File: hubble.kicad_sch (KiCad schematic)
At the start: 97 parts, among them J1 USB3_A_LCSC, J2 USB3_A_LCSC, J3 USB_C_Receptacle_Molex, J5 USB3_A_LCSC, J6 USB3_A_LCSC, J7 USB3_A_LCSC, J8 USB3_A_LCSC, J9 Conn_02x02_Odd_Even, SW1 K3-2235D-F1, U1 MAX6816EUS+T, U10 TPD1E05U06DPY, U11 TPD1E05U06DPY, U12 TPD1E05U06DPY, U13 TPD1E05U06DPY, U2 TPD1E05U06DPY, U3 TS3USB221RSER, U4 TPS7A5201QRGRRQ1, U5 USB5744, U6 TPS7A5201QRGRRQ1, U7 FUSB340, U8 TPD1E05U06DPY, U9 TPD1E05U06DPY, Y1 X322525MOB4SI

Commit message: Add ki-lime-pi-to-go submodule, upgrade to KiCad 9, put a Pico W and through hole header on the schematic
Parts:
- added A1: RaspberryPi_Pico_W, Module_RaspberryPi_Pico:RaspberryPi_Pico_Common_THT, symbol MCU_Module_RaspberryPi_Pico:RaspberryPi_Pico_W_SecondaryPins
- added J10: Pico_Socket_B, Module_RaspberryPi_Pico:RaspberryPi_Pico_PinSocket_1x20_P2.54mm_Vertical, symbol MCU_Module_RaspberryPi_Pico:RaspberryPi_Pico_MultiPart-Socket_B
- added J4: Pico_Socket_A, Module_RaspberryPi_Pico:RaspberryPi_Pico_PinSocket_1x20_P2.54mm_Vertical, symbol MCU_Module_RaspberryPi_Pico:RaspberryPi_Pico_MultiPart-Socket_A
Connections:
- new net: A1.1 (GPIO0), J4.1 (GPIO0)
- new net: A1.10 (GPIO7), J4.10 (GPIO7)
- new net: A1.11 (GPIO8), J4.11 (GPIO8)
- new net: A1.12 (GPIO9), J4.12 (GPIO9)
- new net: A1.13 (GND), A1.18 (GND), A1.23 (GND), A1.28 (GND), A1.3 (GND), A1.38 (GND), A1.8 (GND), A1.D2 (GND), J10.18 (GND), J10.3 (GND), J10.8 (GND), J4.13 (GND), J4.18 (GND), J4.3 (GND), J4.8 (GND)
- new net: A1.14 (GPIO10), J4.14 (GPIO10)
- new net: A1.15 (GPIO11), J4.15 (GPIO11)
- new net: A1.16 (GPIO12), J4.16 (GPIO12)
- new net: A1.17 (GPIO13), J4.17 (GPIO13)
- new net: A1.19 (GPIO14), J4.19 (GPIO14)
- new net: A1.2 (GPIO1), J4.2 (GPIO1)
- new net: A1.20 (GPIO15), J4.20 (GPIO15)
- new net: A1.4 (GPIO2), J4.4 (GPIO2)
- new net: A1.5 (GPIO3), J4.5 (GPIO3)
- new net: A1.6 (GPIO4), J4.6 (GPIO4)
- new net: A1.7 (GPIO5), J4.7 (GPIO5)
- new net: A1.9 (GPIO6), J4.9 (GPIO6)
- new net: A1.21 (GPIO16), J10.1 (GPIO16)
- new net: A1.30 (RUN), J10.10 (RUN)
- new net: A1.31 (GPIO26_ADC0), J10.11 (GPIO26_ADC0)
- new net: A1.32 (GPIO27_ADC1), J10.12 (GPIO27_ADC1)
- new net: A1.33 (AGND), J10.13 (AGND)
- new net: A1.34 (GPIO28_ADC2), J10.14 (GPIO28_ADC2)
- new net: A1.35 (ADC_VREF), J10.15 (ADC_VREF)
- new net: A1.36 (3V3), J10.16 (3V3)
- new net: A1.37 (3V3_EN), J10.17 (3V3_EN)
- new net: A1.39 (VSYS), J10.19 (VSYS)
- new net: A1.22 (GPIO17), J10.2 (GPIO17)
- new net: A1.40 (VBUS), J10.20 (VBUS)
- new net: A1.24 (GPIO18), J10.4 (GPIO18)
- new net: A1.25 (GPIO19), J10.5 (GPIO19)
- new net: A1.26 (GPIO20), J10.6 (GPIO20)
- new net: A1.27 (GPIO21), J10.7 (GPIO21)
- new net: A1.29 (GPIO22), J10.9 (GPIO22)
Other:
- moved on the sheet: C1, C10, C11, C12, C13, C14, C15, C16, C17, C18, C19, C2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

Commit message: Add 2:1 displayport mux using TS3DV642
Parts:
- removed J9: Conn_02x02_Odd_Even, Connector_PinHeader_2.54mm:PinHeader_2x02_P2.54mm_Vertical, symbol Connector_Generic:Conn_02x02_Odd_Even
- added C49, C5, C50, C51, C52, C53, C54, C55: 0.1uF, Capacitor_SMD:C_0603_1608Metric, symbol Device:C_Small
- added J11, J12, J9: DisplayPort, hubble:DISPLAYPORT_XDPF-0205-20S, symbol hubble:DisplayPort
- added R11, R25: 10k, Resistor_SMD:R_0603_1608Metric, symbol Device:R
- added R12, R28: 1M, Resistor_SMD:R_0603_1608Metric, symbol Device:R
- added R26, R27: 100k, Resistor_SMD:R_0603_1608Metric, symbol Device:R
- added R29, R6, R9: 330, Resistor_SMD:R_0603_1608Metric, symbol Device:R
- added TP10, TP11, TP12, TP13, TP14, TP8, TP9: TestPoint, TestPoint:TestPoint_Pad_1.0x1.0mm, symbol Connector:TestPoint
- added U14: TS3DV642A0RUAR, hubble:TS3DV642, symbol hubble:TS3DV642A0RUAR
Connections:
- net GND: now also C49.1, C5.1, C50.1, C55.1, J11.11 (GND), J11.16 (GND), J11.2 (GND), J11.5 (GND), J11.8 (GND), J12.19 (DP_PWR_RET), J12.SH, J9.11 (GND), J9.16 (GND), J9.2 (GND), J9.5 (GND), J9.8 (GND), R11.2, R12.2, R26.2, R28.2, R29.2, R6.2, R9.2, U14.43 (GND)
- net I2C_SCL: now also R14.2; no longer R17.2
- net I2C_SDA: now also R17.2; no longer R14.2
- net MUX_SEL: now also R11.1, U14.17 (SEL2)
- net Shield: now also C49.2, C5.2, C55.2, J11.SH, J12.11 (GND), J12.16 (GND), J12.2 (GND), J12.5 (GND), J12.8 (GND), J9.SH, R29.1, R6.1, R9.1
- net VCC_3.3V: now also C50.2, J12.20 (DP_PWR), R25.1, R27.1, U14.1 (VCC), U14.2 (EN)
- new net: J11.13 (CFG1), TP11.1
- new net: J11.14 (CFG2), TP12.1
- new net: C54.1, J11.15 (AUX_P)
- new net: C53.1, J11.17 (AUX_N)
- new net: J12.13 (CFG1), R28.1
- new net: J9.14 (CFG2), TP14.1
- new net: C51.1, J9.15 (AUX_P)
- new net: J12.14 (CFG2), R12.1
- new net: TP9.1, U14.20 (CEC_B)
- new net: C52.1, J9.17 (AUX_N)
- new net: TP10.1, U14.15 (CEC)
- new net: R25.2, U14.16 (SEL1)
- new net: TP8.1, U14.18 (CEC_A)
- new net: J9.13 (CFG1), TP13.1
- new net DP_HOST0_AUX_N: C52.2, U14.41 (SDA_A)
- new net DP_HOST0_AUX_P: C51.2, U14.42 (SCL_A)
- new net DP_HOST0_D0_N: J9.3 (D0_N), U14.37 (D0-A)
- new net DP_HOST0_D0_P: J9.1 (D0_P), U14.38 (D0+A)
- new net DP_HOST0_D1_N: J9.6 (D1_N), U14.35 (D1-A)
- new net DP_HOST0_D1_P: J9.4 (D1_P), U14.36 (D1+A)
- new net DP_HOST0_D2_N: J9.9 (D2_N), U14.33 (D2-A)
- new net DP_HOST0_D2_P: J9.7 (D2_P), U14.34 (D2+A)
- new net DP_HOST0_D3_N: J9.12 (D3_N), U14.31 (D3-A)
- new net DP_HOST0_D3_P: J9.10 (D3_P), U14.32 (D3+A)
- new net DP_HOST0_HPD: J9.18 (HPD), U14.19 (HPD_A)
- new net DP_HOST1_AUX_N: C53.2, U14.39 (SDA_B)
- new net DP_HOST1_AUX_P: C54.2, U14.40 (SCL_B)
- new net DP_HOST1_D0_N: J11.3 (D0_N), U14.28 (D0-B)
- new net DP_HOST1_D0_P: J11.1 (D0_P), U14.29 (D0+B)
- new net DP_HOST1_D1_N: J11.6 (D1_N), U14.26 (D1-B)
- new net DP_HOST1_D1_P: J11.4 (D1_P), U14.27 (D1+B)
- new net DP_HOST1_D2_N: J11.9 (D2_N), U14.24 (D2-B)
- new net DP_HOST1_D2_P: J11.7 (D2_P), U14.25 (D2+B)
- new net DP_HOST1_D3_N: J11.12 (D3_N), U14.22 (D3-B)
- new net DP_HOST1_D3_P: J11.10 (D3_P), U14.23 (D3+B)
- new net DP_HOST1_HPD: J11.18 (HPD), U14.21 (HPD_B)
- new net DP_SINK_AUX_N: J12.17 (AUX_N), R27.2, U14.4 (SDA)
- new net DP_SINK_AUX_P: J12.15 (AUX_P), R26.1, U14.3 (SCL)
- new net DP_SINK_D0_N: J12.12 (D3_N), U14.6 (D0-)
- new net DP_SINK_D0_P: J12.10 (D3_P), U14.5 (D0+)
- new net DP_SINK_D1_N: J12.9 (D2_N), U14.8 (D1-)
- new net DP_SINK_D1_P: J12.7 (D2_P), U14.7 (D1+)
- new net DP_SINK_D2_N: J12.6 (D1_N), U14.11 (D2-)
- new net DP_SINK_D2_P: J12.4 (D1_P), U14.10 (D2+)
- new net DP_SINK_D3_N: J12.3 (D0_N), U14.13 (D3-)
- new net DP_SINK_D3_P: J12.1 (D0_P), U14.12 (D3+)
- new net DP_SINK_HPD: J12.18 (HPD), U14.14 (HPD)
- no-connect marks 21 -> 26
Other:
- note added: "HOST0 by default"
- note added: "Since we have 2 cables, un-flip the data lanes"
- note added: "TODO: check these PUs/PDs"
- note removed: "Shortened TotalPhase Aardvark debug connector"
- moved on the sheet: A1, C1, C10, C11, C12, C13, C14, C15, C16, C17, C18, C19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

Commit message: Use 2x FUSB340 mux for DisplayPort, break up schematic into hierarchical pages
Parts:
- removed A1: RaspberryPi_Pico_W, Module_RaspberryPi_Pico:RaspberryPi_Pico_Common_THT, symbol MCU_Module_RaspberryPi_Pico:RaspberryPi_Pico_W_SecondaryPins
- removed C1, C10, C11, C12, C14, C15, C16, C17, C18, C19, C20, C21, C22, C23, C24, C25, C27, C28, C29, C30, C31, C32, C34, C35, C37, C38, C39, C40, C41, C42, C43, C44, C49, C5, C50, C51, C52, C53, C54, C55, C6, C7, C8, C9: 0.1uF, Capacitor_SMD:C_0603_1608Metric, symbol Device:C_Small
- removed C13, C33: 10uF, Capacitor_SMD:C_0603_1608Metric, symbol Device:C_Small
- removed C2, C45, C46, C47, C48: 2.2uF, Capacitor_SMD:C_0603_1608Metric, symbol Device:C_Small
- removed C26, C36: 22uF, Capacitor_SMD:C_0603_1608Metric, symbol Device:C_Small
- removed C3, C4: 20pF, Capacitor_SMD:C_0603_1608Metric, symbol Device:C_Small
- removed J1, J2, J5, J6, J7, J8: USB3_A_LCSC, hubble:USB-TH_XUNPU_USB-301WD-ARY, symbol hubble:USB3_A_LCSC
- removed J10: Pico_Socket_B, Module_RaspberryPi_Pico:RaspberryPi_Pico_PinSocket_1x20_P2.54mm_Vertical, symbol MCU_Module_RaspberryPi_Pico:RaspberryPi_Pico_MultiPart-Socket_B
- removed J11, J12, J9: DisplayPort, hubble:DISPLAYPORT_XDPF-0205-20S, symbol hubble:DisplayPort
- removed J3: USB_C_Receptacle_Molex, hubble:USB_C_CONN_105450-0101_MOLEX, symbol hubble:USB_C_Receptacle_Molex
- removed J4: Pico_Socket_A, Module_RaspberryPi_Pico:RaspberryPi_Pico_PinSocket_1x20_P2.54mm_Vertical, symbol MCU_Module_RaspberryPi_Pico:RaspberryPi_Pico_MultiPart-Socket_A
- removed R1, R29, R6, R9: 330, Resistor_SMD:R_0603_1608Metric, symbol Device:R
- removed R10, R11, R13, R14, R17, R25: 10k, Resistor_SMD:R_0603_1608Metric, symbol Device:R
- removed R12, R28: 1M, Resistor_SMD:R_0603_1608Metric, symbol Device:R
- removed R15: 11.8k, Resistor_SMD:R_0603_1608Metric, symbol Device:R
- removed R16: 3.74k, Resistor_SMD:R_0603_1608Metric, symbol Device:R
- removed R18, R24, R7: 50k, Resistor_SMD:R_0603_1608Metric, symbol Device:R
- removed R19: 12k, Resistor_SMD:R_0603_1608Metric, symbol Device:R
- removed R2, R3: 5.1k, Resistor_SMD:R_0603_1608Metric, symbol Device:R
- removed R20, R21: 200k, Resistor_SMD:R_0603_1608Metric, symbol Device:R
- removed R22: 12.4k, Resistor_SMD:R_0603_1608Metric, symbol Device:R
- removed R23: 24.9k, Resistor_SMD:R_0603_1608Metric, symbol Device:R
- removed R26, R27, R8: 100k, Resistor_SMD:R_0603_1608Metric, symbol Device:R
- removed R4, R5: 0, Resistor_SMD:R_0603_1608Metric, symbol Device:R
- removed SW1: K3-2235D-F1, hubble:SW-TH_K3-2235D-F1, symbol Switch:SW_Push_DPDT
- removed TP1, TP10, TP11, TP12, TP13, TP14, TP2, TP3, TP4, TP5, TP6, TP7, TP8, TP9: TestPoint, TestPoint:TestPoint_Pad_1.0x1.0mm, symbol Connector:TestPoint
- removed U1: MAX6816EUS+T, Package_TO_SOT_SMD:SOT-143, symbol Interface:MAX6816
- removed U10, U11, U12, U13, U2, U8, U9: TPD1E05U06DPY, Package_SON:Texas_DPY0002A_0.6x1mm_P0.65mm, symbol Power_Protection:TPD1E05U06DPY
- removed U14: TS3DV642A0RUAR, hubble:TS3DV642, symbol hubble:TS3DV642A0RUAR
- removed U3: TS3USB221RSER, hubble:UQFN-10, symbol hubble:SN080104RSER
- removed U4, U6: TPS7A5201QRGRRQ1, hubble:RGR20_2P05X2P05_TEX, symbol hubble:TPS7A5201QRGRRQ1
- removed U5: USB5744, hubble:VQFN56_2G_MCH, symbol hubble:USB5744-I_2G
- removed U7: FUSB340, hubble:TMLP-18_L2.8-W2.0-P0.40-BL-EP, symbol hubble:FUSB340TMX
- removed Y1: X322525MOB4SI, Crystal:Crystal_SMD_3225-4Pin_3.2x2.5mm, symbol Device:Crystal_GND24_Small
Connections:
- no-connect marks 26 -> 0
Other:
- added sheet DisplayPort (displayport.kicad_sch)
- added sheet Hub (hub.kicad_sch)
- added sheet MCU (mcu.kicad_sch)
- added sheet Power (power.kicad_sch)
- note removed: "1%"
- note removed: "1.2V LDO"
- note removed: "1D+/- by default"
- note removed: "25MHz"
- note removed: "3.3V LDO"
- note removed: "HOST 1"
- note removed: "HOST 2"
- note removed: "HOST0 by default"
- note removed: "IN"
- note removed: "If I get bored and want to make a USB-C debug board..."
- note removed: "Not using a PD controller for now Assuming Type-C power supplies simply have enough oomph"
- note removed: "OUT"
- note removed: "Since we have 2 cables, un-flip the data lanes"
- note removed: "TODO: check these PUs/PDs"
- note removed: "TX1/RX1 by default"
- note removed: "VBUS_DET into USB5744 should be 3.3V or 0V"

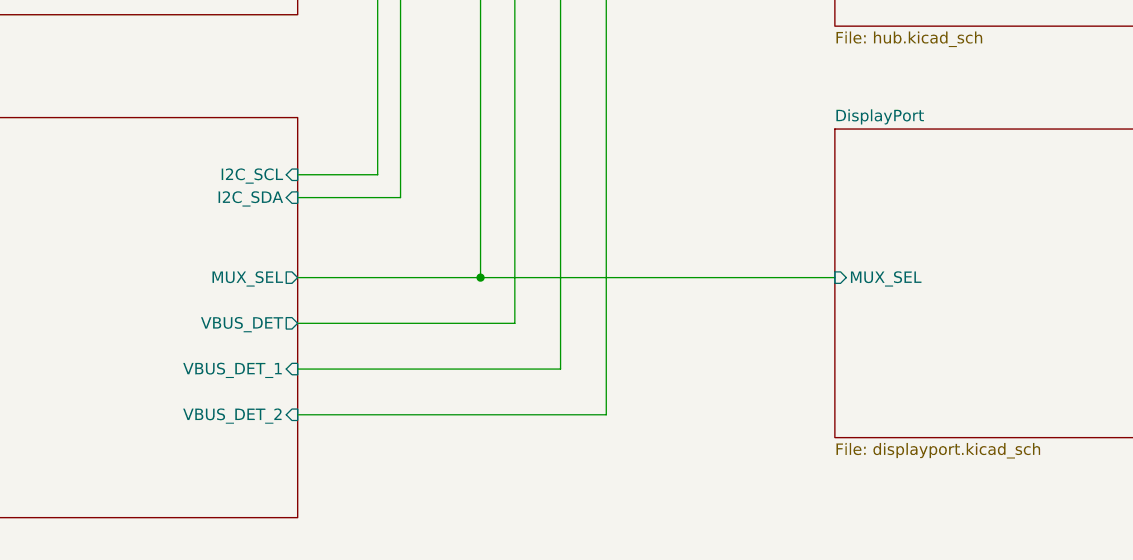
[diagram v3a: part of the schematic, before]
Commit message: Start wiring up Pi Pico
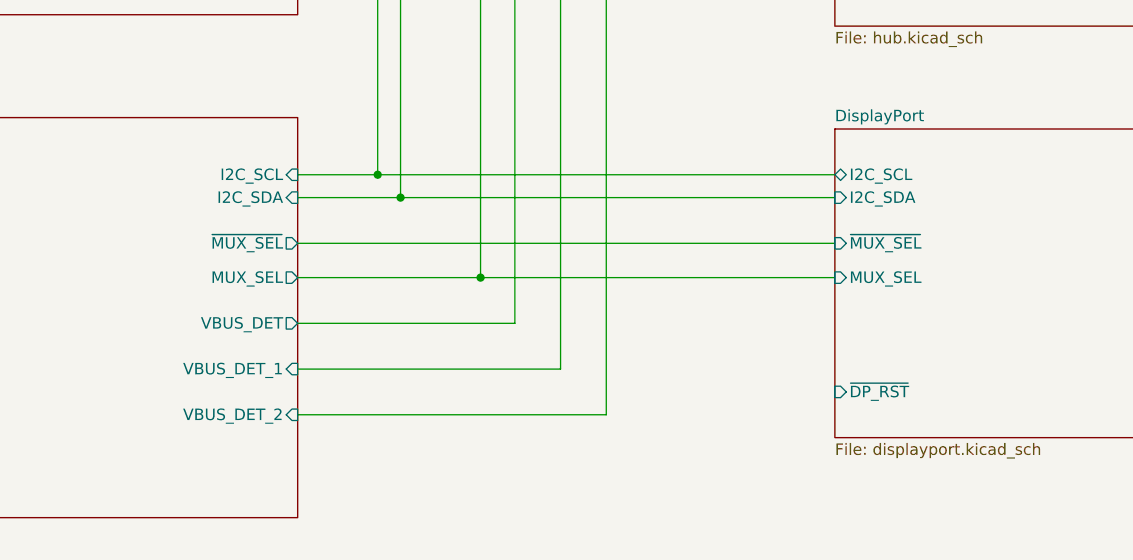
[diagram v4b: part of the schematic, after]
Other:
- sheet DisplayPort ports: added I2C_SCL, I2C_SDA, ~{DP_RST}, ~{MUX_SEL}; removed none
- sheet MCU ports: added ~{MUX_SEL}; removed none
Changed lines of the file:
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@@
+	)
+	(junction
+		(at 205.74 160.02)
+		(diameter 0)
+		(color 0 0 0 0)
 	)
 	(junction
@@
 	)
 	(junction
+		(at 203.2 157.48)
+		(diameter 0)
+		(color 0 0 0 0)
+	)
+	(junction
 		(at 214.63 168.91)
 		(diameter 0)
@@
 	(wire
 		(pts
+			(xy 194.31 165.1) (xy 254 165.1)
+		)
+		(stroke
+			(width 0)
+			(type default)
+		)
+	)
+	(wire
+		(pts
 			(xy 214.63 168.91) (xy 254 168.91)
 		)
@@
 	(wire
 		(pts
+			(xy 203.2 157.48) (xy 254 157.48)
+		)
+		(stroke
+			(width 0)
+			(type default)
+		)
+	)
+	(wire
+		(pts
 			(xy 194.31 179.07) (xy 223.52 179.07)
 		)
@@
 		(pts
 			(xy 254 119.38) (xy 218.44 119.38)
+		)
+		(stroke
+			(width 0)
+			(type default)
+		)
+	)
+	(wire
+		(pts
+			(xy 205.74 160.02) (xy 254 160.02)
 		)
 		(stroke
@@
 			)
 		)
+		(pin "I2C_SCL" bidirectional
+			(at 254 157.48 180)
+			(effects
+				(font
+					(size 1.27 1.27)
+				)
+				(justify left)
+			)
+		)
+		(pin "I2C_SDA" input
+			(at 254 160.02 180)
+			(effects
+				(font
+					(size 1.27 1.27)
+				)
+				(justify left)
+			)
+		)
+		(pin "~{DP_RST}" input
+			(at 254 181.61 180)
+			(effects
+				(font
+					(size 1.27 1.27)
+				)
+				(justify left)
+			)
+		)
+		(pin "~{MUX_SEL}" input
+			(at 254 165.1 180)
+			(effects
+				(font
+					(size 1.27 1.27)
+				)
+				(justify left)
+			)
+		)
 		(instances
 			(project "hubble"
@@
 			(effects
 				(font
+					(size 1.27 1.27)
+				)
+				(justify right)
+			)
+		)
+		(pin "~{MUX_SEL}" output
+			(at 194.31 165.1 0)
+			(effects
+				(font
